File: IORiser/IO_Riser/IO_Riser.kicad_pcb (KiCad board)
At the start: 2 copper layers, 58 x 90 mm, 6 parts, among them J1 I/O Port, J2 I/O Port

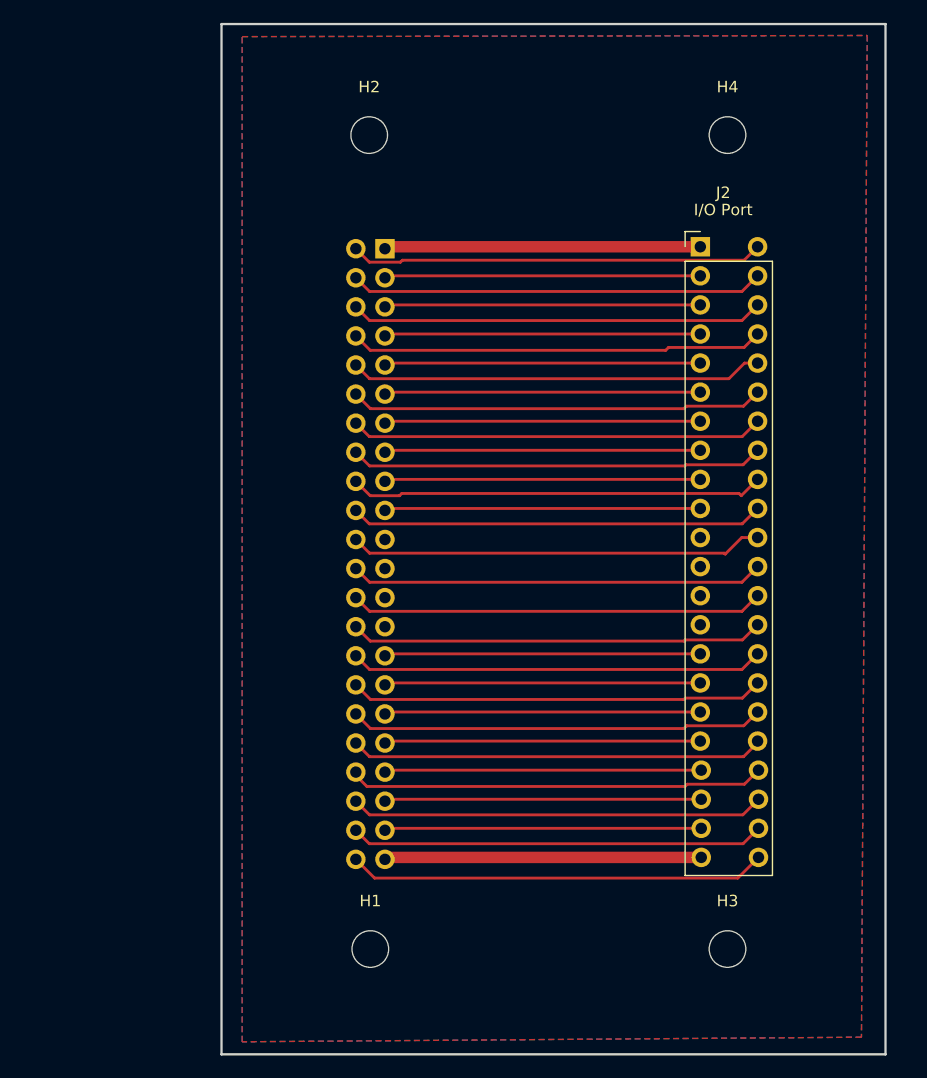
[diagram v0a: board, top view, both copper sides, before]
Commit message: rework IO Riser
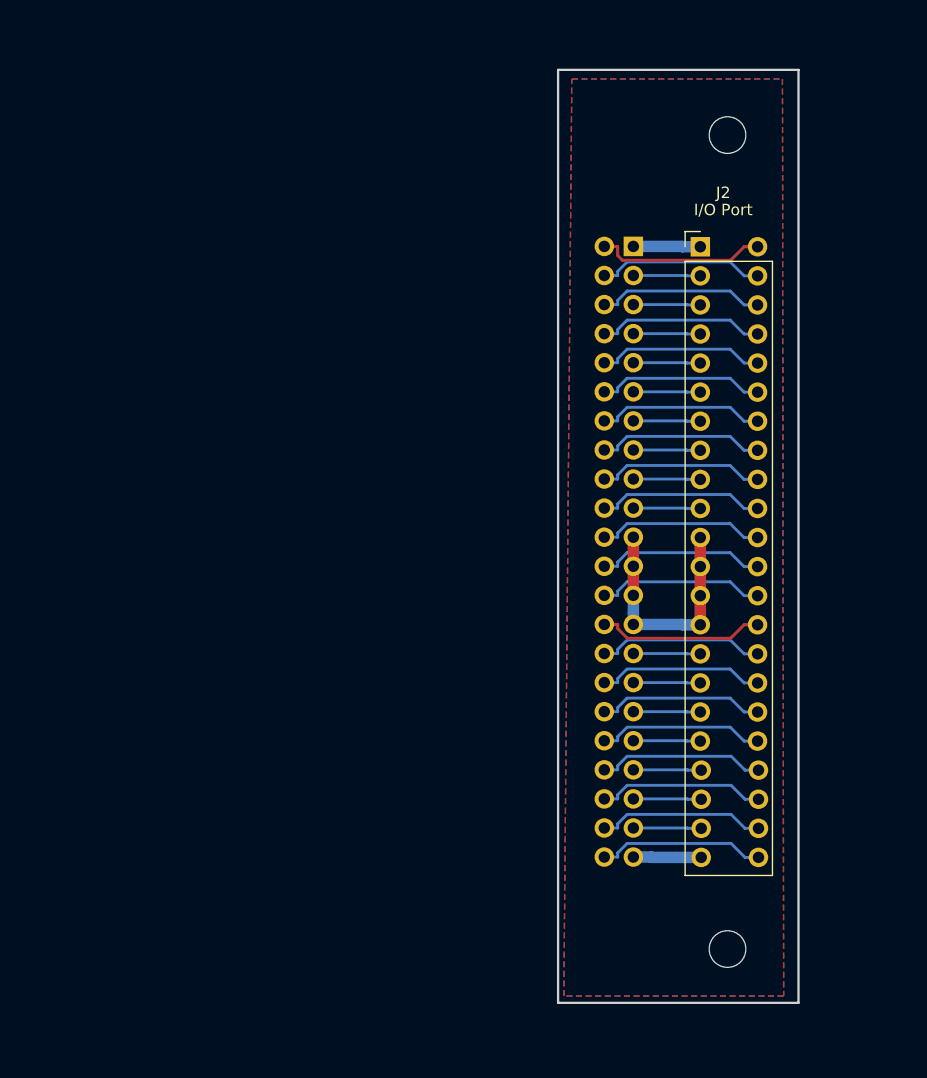
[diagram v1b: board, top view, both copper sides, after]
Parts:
- removed H1, H2: MountingHole, MountingHole:MountingHole_3.2mm_M3
- moved J1 21.7 mm to (146.0, 58.4)
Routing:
- net IO_SNDIN: track 36.6 -> 14.7 mm
- net D5: track 36.4 -> 14.7 mm
- net IO_A9: track 36.4 -> 14.6 mm
- net ~{IO_LOAD}: track 27.6 -> 5.86 mm
- net ~{IO_RESET}: track 27.6 -> 5.86 mm
- net IO_A5: track 27.6 -> 5.86 mm
- net IO_DBIN: track 27.6 -> 5.86 mm
- net IO_CRUIN: track 27.6 -> 5.86 mm
- net IO_A6: track 27.6 -> 5.86 mm
- net IO_A4: track 27.6 -> 5.86 mm
- net IO_A15-CRUOUT: track 27.6 -> 5.86 mm
- net IO_A13: track 27.6 -> 5.86 mm
- net IO_A12: track 27.6 -> 5.86 mm
- net HOLD/IAQ: track 27.7 -> 5.94 mm
- net D4: track 27.6 -> 5.86 mm
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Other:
- board size 58 x 90 mm -> 21 x 81.5 mm

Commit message: Add BOM
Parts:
- J1: moved to F.Cu
- J2: footprint WernerCustomLibrary:Card_edge_44 -> WernerCustomLibrary:44 Pin Card Edge
- moved J2 72.0 mm to (154.5, 126.2), turned to 90 degrees
- moved J1 3.22 mm to (143.0, 57.2), turned to 0 degrees
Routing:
- net GND: track 21.1 -> 0.00 mm
- net SBE: track 14.8 -> 0.00 mm
- net IO_SNDIN: track 14.7 -> 0.00 mm
- net D1: track 14.7 -> 0.00 mm
- net D5: track 14.7 -> 0.00 mm
- net D3: track 14.7 -> 0.00 mm
- net D6: track 14.6 -> 0.00 mm
- net ~{MEMEN}: track 14.6 -> 0.00 mm
- net ~{IO_CRUCLK}: track 14.6 -> 0.00 mm
- net IO_A14: track 14.6 -> 0.00 mm
- net D7: track 14.6 -> 0.00 mm
- net ~{IO_WE}: track 14.6 -> 0.00 mm
- net READY_~{HOLD}: track 14.6 -> 0.00 mm
- net IO_A9: track 14.6 -> 0.00 mm
- net IO_A11: track 14.6 -> 0.00 mm
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- removed copper zone on B.Cu, net GND
- removed copper zone on F.Cu, net GND
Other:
- board size 21 x 81.5 mm -> 29.9 x 82.4 mm

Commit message: PCB updates
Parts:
- moved J1 53.3 mm to (97.8, 85.5), turned to 90 degrees
- moved H3 18.7 mm to (145.5, 103.2)
- moved H4 17.5 mm to (145.5, 63.9)
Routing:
- net SBE: track 0.00 -> 83.7 mm
- net ~{IO_EXT_INT}: track 0.00 -> 79.5 mm
- net +5V: track 0.00 -> 78.6 mm
- net IO_A10: track 0.00 -> 75.9 mm
- net ~{IO_RESET}: track 0.00 -> 75.0 mm
- net IO_A11: track 0.00 -> 73.5 mm
- net IO_A5: track 0.00 -> 71.4 mm
- net IO_A4: track 0.00 -> 69.0 mm
- net IO_A3: track 0.00 -> 68.7 mm
- net READY_~{HOLD}: track 0.00 -> 65.1 mm
- net IO_DBIN: track 0.00 -> 64.2 mm
- net IO_A8: track 0.00 -> 61.5 mm
- net IO_A12: track 0.00 -> 60.6 mm
- net GND: track 0.00 -> 59.6 mm
- net IO_A14: track 0.00 -> 57.9 mm
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- added copper zone on B.Cu, net GND
- added copper zone on F.Cu, net GND
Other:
- board size 29.9 x 82.4 mm -> 76.9 x 58.5 mm
